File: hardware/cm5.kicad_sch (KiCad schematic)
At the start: 6 parts, among them J7 Conn_02x07_Odd_Even, J9 Conn_02x08_Odd_Even

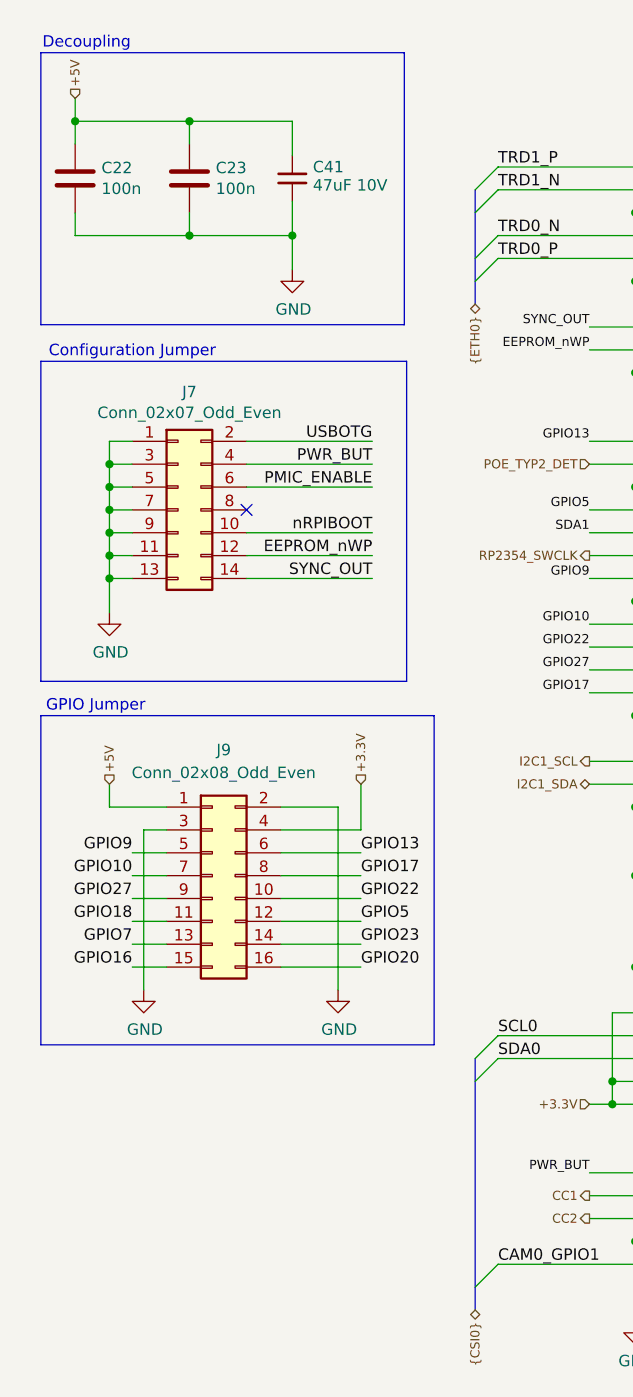
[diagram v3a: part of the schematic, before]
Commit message: Add switchable ESC power, vertical camera connectors and 3.3 V decoupling
- ESC power switch on the root sheet:
  - Battery input J6 changes to XT60PW-M. New XT60PW-F J14 carries switched
    power to both ESCs.
  - Q3 (onsemi NTMFS5C404NLT1G, 40 V, 0.67 mOhm) is driven by the photovoltaic
    driver IC16 (Vishay VOM1271T) from RP2354A GPIO14 (ESC_PWR_EN) via R31.
  - Soft start C46/D6/R32 keeps Q3 in its SOA while the ESC capacitors charge.
    D7 clamps the gate when the battery is unplugged or the thrusters windmill.
  - Static switch with no current limit: the battery BMS protects. Firmware
    timing rules are in the schematic note and the README.
- Camera connectors J5/J11 are now Molex 501951-2230 (vertical, flip lock).
  The footprint numbers pads n = Molex circuit 23-n so a standard Pi 22-pin
  cable lands GND on pin 1, as on the CM5 IO Board.
- Decoupling: 10 uF + 100 nF at the CM5 3.3 V output, 10 uF at each camera
  supply pin.
- Polyfuses F1-F3 removed; the battery feeds the charger path directly.
- New libraries VOM1271T, NTMFS5C404NL, Molex and Vishay, with 3D models.
- PCB updated from the schematic. The layout will be redone.

Co-Authored-By: Claude Opus 5.5 <noreply@anthropic.com>
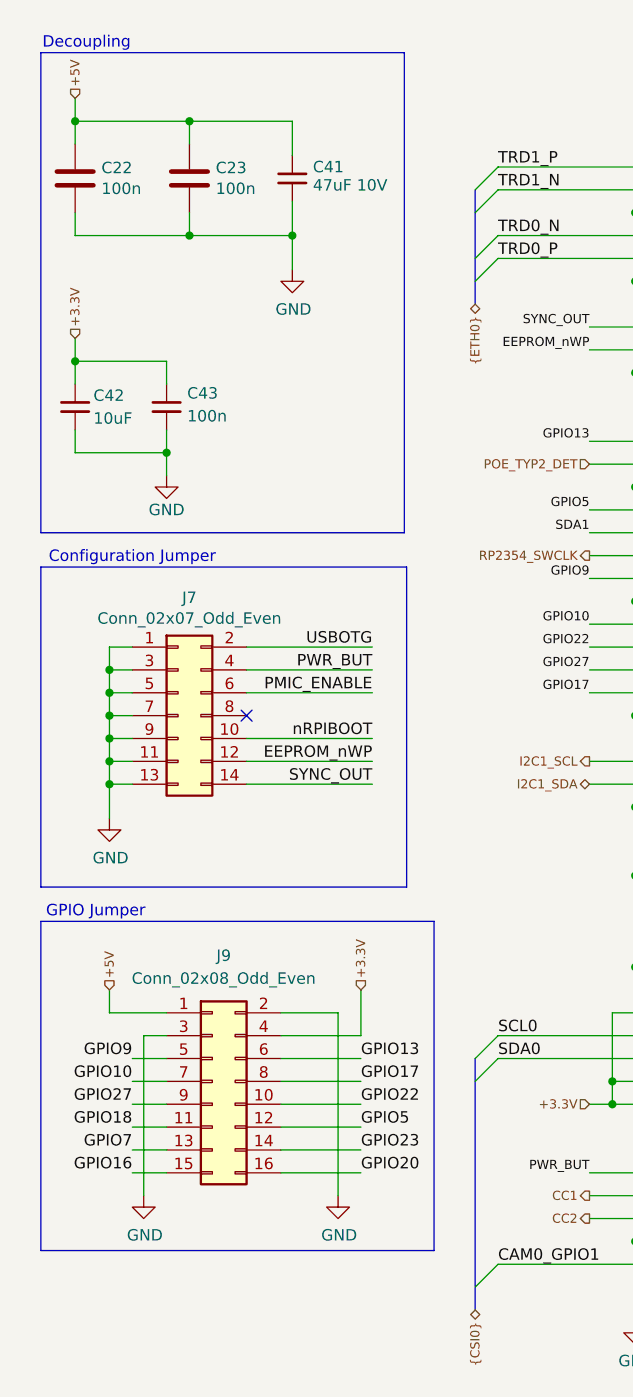
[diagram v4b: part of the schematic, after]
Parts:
- added C42: 10uF, Capacitor_SMD:C_0603_1608Metric, symbol Device:C_Small
- added C43: 100n, Capacitor_SMD:C_0402_1005Metric, symbol Device:C_Small
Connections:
- net +3.3V: now also C42.1, C43.1
- net GND: now also C42.2, C43.2
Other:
- moved on the sheet: J7, J9
